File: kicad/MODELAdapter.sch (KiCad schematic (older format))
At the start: 0 parts

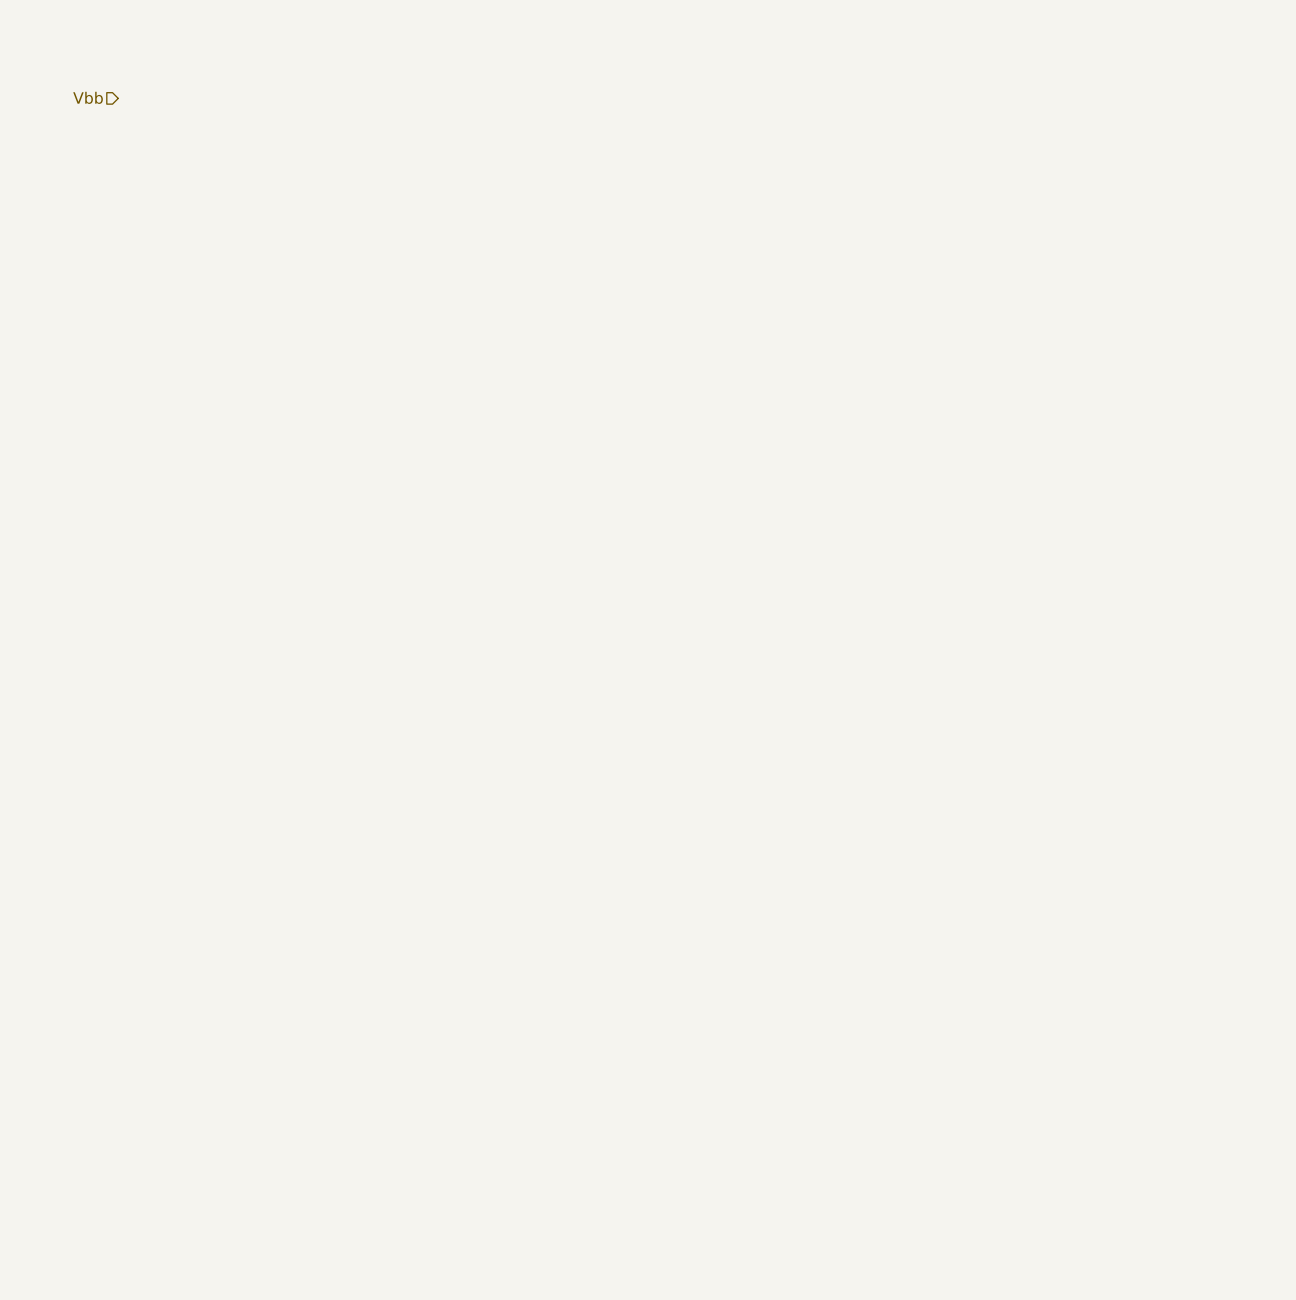
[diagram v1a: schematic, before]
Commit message: Added some more detail and moved the display from SPI to I2C
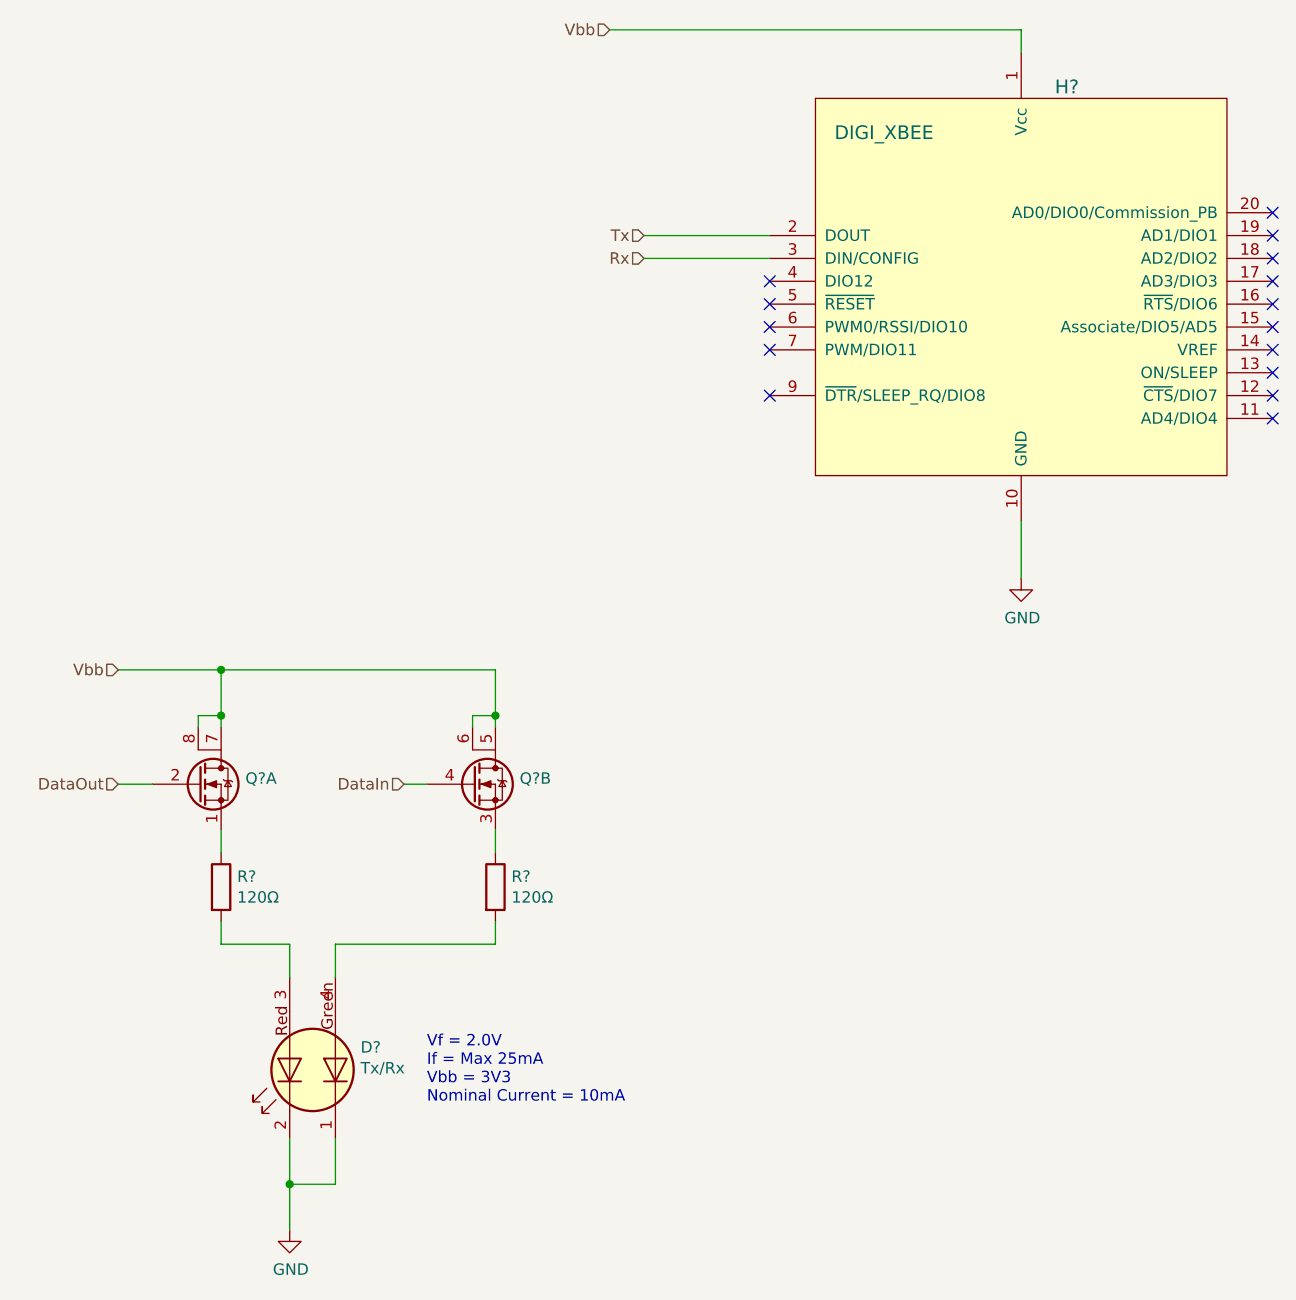
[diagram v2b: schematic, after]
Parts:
- added D?: Tx/Rx, symbol FieldDevice_R2:LED_Dual_CCAA
- added H?: DIGI_XBEE, symbol FieldDevice_R2:DIGI_XBEE
- added Q? (x2): Q_DUAL_NMOS_G2D78S1G4D56S3, symbol FieldDevice_R2:Q_DUAL_NMOS_G2D78S1G4D56S3
- added R? (x2): 120Ω, symbol Device:R
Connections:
- net Vbb: now also H?.1 (Vcc), Q?.5 (D), Q?.6 (D), Q?.7 (D), Q?.8 (D)
- new net: Q?.1 (S), R?.1
- new net: D?.3 (K1), R?.2
- new net: Q?.3 (S), R?.1
- new net: D?.4 (K2), R?.2
- new net DataIn: Q?.4 (G)
- new net DataOut: Q?.2 (G)
- new net GND: D?.1 (A1), D?.2 (A2), H?.10 (GND)
- new net Rx: H?.3 (DIN/CONFIG)
- new net Tx: H?.2 (DOUT)
- no-connect marks 0 -> 15
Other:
- note added: "Vf = 2.0V\nIf = Max 25mA\nVbb = 3V3\nNominal Current = 10mA"
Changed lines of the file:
@@
 EESchema Schematic File Version 4
 LIBS:FieldDevice_R2-cache
-LIBS:FieldDevice_Power_5V-cache
-EELAYER 26 0
+EELAYER 29 0
 EELAYER END
 $Descr A4 11693 8268
 encoding utf-8
-Sheet 8 8
+Sheet 7 8
 Title ""
 Date ""
@@
 Comment4 ""
 $EndDescr
-Text HLabel 2150 1650 0    50   Input ~ 0
+Text HLabel 4300 1350 0    50   Input ~ 0
 Vbb
+Text HLabel 4450 2350 0    50   Input ~ 0
+Rx
+Text HLabel 4450 2250 0    50   Input ~ 0
+Tx
+$Comp
+L FieldDevice_R2:DIGI_XBEE H?
+U 1 1 5CBC3B62
+P 6100 2500
+F 0 "H?" H 6300 3400 60  0000 C CNN
+F 1 "DIGI_XBEE" H 5500 3200 60  0000 C CNN
+F 2 "" H 5450 2300 60  0000 C CNN
+F 3 "" H 5450 2300 60  0000 C CNN
+	1    6100 2500
+	1    0    0    -1
+$EndComp
+Wire Wire Line
+	4300 1350 6100 1350
+Wire Wire Line
+	6100 1350 6100 1450
+Wire Wire Line
+	6100 3500 6100 3750
+$Comp
+L FieldDevice_Power_5V-rescue:GND #PWR?
+U 1 1 5CBC5560
+P 6100 3750
+F 0 "#PWR?" H 6100 3500 50  0001 C CNN
+F 1 "GND" H 6105 3577 50  0000 C CNN
+F 2 "" H 6100 3750 50  0001 C CNN
+F 3 "" H 6100 3750 50  0001 C CNN
+	1    6100 3750
+	1    0    0    -1
+$EndComp
+Wire Wire Line
+	5000 2250 4450 2250
+Wire Wire Line
+	5000 2350 4450 2350
+NoConn ~ 5000 2450
+NoConn ~ 5000 2550
+NoConn ~ 5000 2650
+NoConn ~ 5000 2750
+NoConn ~ 5000 2950
+NoConn ~ 7200 3050
+NoConn ~ 7200 2950
+NoConn ~ 7200 2850
+NoConn ~ 7200 2750
+NoConn ~ 7200 2650
+NoConn ~ 7200 2550
+NoConn ~ 7200 2450
+NoConn ~ 7200 2350
+NoConn ~ 7200 2250
+NoConn ~ 7200 2150
+Text HLabel 2150 4150 0    50   Input ~ 0
+Vbb
+Wire Wire Line
+	2150 4150 2600 4150
+Wire Wire Line
+	2600 4150 2600 4350
+Wire Wire Line
+	2600 4150 3800 4150
+Wire Wire Line
+	3800 4150 3800 4350
+Connection ~ 2600 4150
+$Comp
+L Device:R R?
+U 1 1 5CBCC41D
+P 2600 5100
+F 0 "R?" H 2670 5146 50  0000 L CNN
+F 1 "120Ω" H 2670 5055 50  0000 L CNN
+F 2 "" V 2530 5100 50  0001 C CNN
+F 3 "~" H 2600 5100 50  0001 C CNN
+	1    2600 5100
+	1    0    0    -1
+$EndComp
+$Comp
+L Device:R R?
+U 1 1 5CBCCB57
+P 3800 5100
+F 0 "R?" H 3870 5146 50  0000 L CNN
+F 1 "120Ω" H 3870 5055 50  0000 L CNN
+F 2 "" V 3730 5100 50  0001 C CNN
+F 3 "~" H 3800 5100 50  0001 C CNN
+	1    3800 5100
+	1    0    0    -1
+$EndComp
+$Comp
+L FieldDevice_R2:LED_Dual_CCAA D?
+U 1 1 5CBD6344
+P 3000 5900
+F 0 "D?" V 3099 5690 50  0000 R CNN
+F 1 "Tx/Rx" V 3008 5690 50  0000 R CNN
+F 2 "" H 2970 5900 50  0001 C CNN
+F 3 "https://cdn-reichelt.de/documents/datenblatt/A500/15-22SURSYGC-S530-A3-E2-TR8_ENG_TDS.pdf" H 2970 5900 50  0001 C CNN
+F 4 "EVL 15-22SURSYG" H 3000 5900 50  0001 C CNN "MPN"
+F 5 "https://www.reichelt.de/led-smd-1210-rot-gruen-54-mcd-120-evl-15-22sursyg-p232060.html?&trstct=pol_1" H 3000 5900 50  0001 C CNN "Link"
+	1    3000 5900
+	0    -1   -1   0
+$EndComp
+$Comp
+L FieldDevice_Power_5V-rescue:GND #PWR?
+U 1 1 5CBC9016
+P 2900 6600
+F 0 "#PWR?" H 2900 6350 50  0001 C CNN
+F 1 "GND" H 2905 6427 50  0000 C CNN
+F 2 "" H 2900 6600 50  0001 C CNN
+F 3 "" H 2900 6600 50  0001 C CNN
+	1    2900 6600
+	1    0    0    -1
+$EndComp
+Wire Wire Line
+	2900 6200 2900 6400
+Wire Wire Line
+	3100 6200 3100 6400
+Wire Wire Line
+	3100 6400 2900 6400
+Connection ~ 2900 6400
+Wire Wire Line
+	2900 6400 2900 6600
+Wire Wire Line
+	2600 5250 2600 5350
+Wire Wire Line
+	2600 5350 2900 5350
+Wire Wire Line
+	3100 5350 3800 5350
+Wire Wire Line
+	3800 5350 3800 5250
+Wire Wire Line
+	2900 5495 2900 5350
+Wire Wire Line
+	3100 5495 3100 5350
+Wire Wire Line
+	3500 4650 3400 4650
+Wire Wire Line
+	2300 4650 2150 4650
+Text HLabel 2150 4650 0    50   Input ~ 0
+DataOut
+Text HLabel 3400 4650 0    50   Input ~ 0
+DataIn
+$Comp
+L FieldDevice_R2:Q_DUAL_NMOS_G2D78S1G4D56S3 Q?
+U 1 1 5CBC91E5
+P 2500 4650
+F 0 "Q?" H 2706 4675 50  0000 L CNN
+F 1 "Q_DUAL_NMOS_G2D78S1G4D56S3" H 2706 4630 50  0001 L CNN
+F 2 "" H 2700 4650 50  0001 C CNN
+F 3 "https://cdn-reichelt.de/documents/datenblatt/A200/TSM9926DCS.pdf" H 2700 4650 50  0001 C CNN
+F 4 "TSM9926DCS " H 2500 4650 50  0001 C CNN "MPN"
+F 5 "https://www.reichelt.de/mosfet-2xn-ch-20v-6a-0-03r-so8-tsm9926dcs-p254992.html?&trstct=pol_0" H 2500 4650 50  0001 C CNN "Link"
+	1    2500 4650
+	1    0    0    -1
+$EndComp
+Wire Wire Line
+	2600 4850 2600 4950
+Wire Wire Line
+	2500 4400 2500 4350
+Wire Wire Line
+	2500 4350 2600 4350
+Connection ~ 2600 4350
+Wire Wire Line
+	2600 4350 2600 4400
+$Comp
+L FieldDevice_R2:Q_DUAL_NMOS_G2D78S1G4D56S3 Q?
+U 2 1 5CBCC7E8
+P 3700 4650
+F 0 "Q?" H 3906 4675 50  0000 L CNN
+F 1 "Q_DUAL_NMOS_G2D78S1G4D56S3" H 3906 4630 50  0001 L CNN
+F 2 "" H 3900 4650 50  0001 C CNN
+F 3 "https://cdn-reichelt.de/documents/datenblatt/A200/TSM9926DCS.pdf" H 3900 4650 50  0001 C CNN
+F 4 "TSM9926DCS " H 3700 4650 50  0001 C CNN "MPN"
+F 5 "https://www.reichelt.de/mosfet-2xn-ch-20v-6a-0-03r-so8-tsm9926dcs-p254992.html?&trstct=pol_0" H 3700 4650 50  0001 C CNN "Link"
+	2    3700 4650
+	1    0    0    -1
+$EndComp
+Wire Wire Line
+	3700 4400 3700 4350
+Wire Wire Line
+	3700 4350 3800 4350
+Connection ~ 3800 4350
+Wire Wire Line
+	3800 4350 3800 4400
+Wire Wire Line
+	3800 4850 3800 4950
+Text Notes 3500 6050 0    50   ~ 0
+Vf = 2.0V\nIf = Max 25mA\nVbb = 3V3\nNominal Current = 10mA
 $EndSCHEMATC

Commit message: Revision 3
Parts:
- D?: Link https://www.reichelt.de/led-smd-1210-rot-gruen-54-mcd-120-e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 -> https://www.digikey.de/product-detail/de/lumex-opto-compone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; MPN EVL 15-22SURSYG -> SML-LX15IGC-RP-TR
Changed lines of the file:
@@
 Comment4 ""
 $EndDescr
-Text HLabel 4300 1350 0    50   Input ~ 0
+Text HLabel 5600 1350 0    50   Input ~ 0
 Vbb
 Text HLabel 4450 2350 0    50   Input ~ 0
@@
 $EndComp
 Wire Wire Line
-	4300 1350 6100 1350
+	5600 1350 6100 1350
 Wire Wire Line
 	6100 1350 6100 1450
@@
 F 1 "Tx/Rx" V 3008 5690 50  0000 R CNN
 F 2 "" H 2970 5900 50  0001 C CNN
-F 3 "https://cdn-reichelt.de/documents/datenblatt/A500/15-22SURSYGC-S530-A3-E2-TR8_ENG_TDS.pdf" H 2970 5900 50  0001 C CNN
-F 4 "EVL 15-22SURSYG" H 3000 5900 50  0001 C CNN "MPN"
-F 5 "https://www.reichelt.de/led-smd-1210-rot-gruen-54-mcd-120-evl-15-22sursyg-p232060.html?&trstct=pol_1" H 3000 5900 50  0001 C CNN "Link"
+F 3 "https://www.lumex.com/spec/SML-LX15IGC-RP-TR.pdf" H 2970 5900 50  0001 C CNN
+F 4 "SML-LX15IGC-RP-TR	" H 3000 5900 50  0001 C CNN "MPN"
+F 5 "https://www.digikey.de/product-detail/de/lumex-opto-components-inc/SML-LX15IGC-RP-TR/67-1655-6-ND/1754501" H 3000 5900 50  0001 C CNN "Link"
 	1    3000 5900
 	0    -1   -1   0

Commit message: Updates and testing
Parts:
- removed Q? (x2): Q_DUAL_NMOS_G2D78S1G4D56S3, symbol FieldDevice_R2:Q_DUAL_NMOS_G2D78S1G4D56S3
- added Q? (x2): Q_DUAL_PMOS_TSM9933DCS, symbol FieldDevice_R2:Q_DUAL_PMOS_TSM9933DCS
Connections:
- net DataIn: now also Q?.4 (G)
- net DataOut: now also Q?.2 (G)
- net Vbb: now also Q?.1 (S), Q?.3 (S)
- net at R?.1: now also Q?.7 (D), Q?.8 (D)
- net at R?.1: now also Q?.5 (D), Q?.6 (D)
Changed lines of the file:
@@
 	2150 4150 2600 4150
 Wire Wire Line
-	2600 4150 2600 4350
-Wire Wire Line
 	2600 4150 3800 4150
-Wire Wire Line
-	3800 4150 3800 4350
 Connection ~ 2600 4150
 $Comp
@@
 	3100 5495 3100 5350
 Wire Wire Line
-	3500 4650 3400 4650
+	2300 4600 2150 4600
+Text HLabel 2150 4600 0    50   Input ~ 0
+DataOut
+Text HLabel 3350 4600 0    50   Input ~ 0
+DataIn
 Wire Wire Line
-	2300 4650 2150 4650
-Text HLabel 2150 4650 0    50   Input ~ 0
-DataOut
-Text HLabel 3400 4650 0    50   Input ~ 0
-DataIn
+	2600 4850 2600 4900
+Wire Wire Line
+	3800 4850 3800 4900
+Text Notes 3500 6050 0    50   ~ 0
+Vf = 2.0V\nIf = Max 25mA\nVbb = 3V3\nNominal Current = 10mA
 $Comp
-L FieldDevice_R2:Q_DUAL_NMOS_G2D78S1G4D56S3 Q?
-U 1 1 5CBC91E5
-P 2500 4650
-F 0 "Q?" H 2706 4675 50  0000 L CNN
-F 1 "Q_DUAL_NMOS_G2D78S1G4D56S3" H 2706 4630 50  0001 L CNN
-F 2 "" H 2700 4650 50  0001 C CNN
-F 3 "https://cdn-reichelt.de/documents/datenblatt/A200/TSM9926DCS.pdf" H 2700 4650 50  0001 C CNN
-F 4 "TSM9926DCS " H 2500 4650 50  0001 C CNN "MPN"
-F 5 "https://www.reichelt.de/mosfet-2xn-ch-20v-6a-0-03r-so8-tsm9926dcs-p254992.html?&trstct=pol_0" H 2500 4650 50  0001 C CNN "Link"
-	1    2500 4650
+L FieldDevice_R2:Q_DUAL_PMOS_TSM9933DCS Q?
+U 1 1 5D6B0A26
+P 2500 4600
+F 0 "Q?" H 2788 4575 50  0000 L CNN
+F 1 "Q_DUAL_PMOS_TSM9933DCS" H 2788 4530 50  0001 L CNN
+F 2 "" H 2550 4600 50  0001 C CNN
+F 3 "https://cdn-reichelt.de/documents/datenblatt/A200/TSM9933DCS.pdf" H 2550 4600 50  0001 C CNN
+F 4 "TSM9933DCS" H 2500 4600 50  0001 C CNN "MPN"
+F 5 "https://www.reichelt.de/mosfet-2xp-ch-20v-4-7a-0-06r-so8-tsm9933dcs-p254993.html?&trstct=pol_0" H 2500 4600 50  0001 C CNN "Link"
+	1    2500 4600
+	1    0    0    -1
+$EndComp
+$Comp
+L FieldDevice_R2:Q_DUAL_PMOS_TSM9933DCS Q?
+U 2 1 5D6B2369
+P 3700 4600
+F 0 "Q?" H 3988 4575 50  0000 L CNN
+F 1 "Q_DUAL_PMOS_TSM9933DCS" H 3988 4530 50  0001 L CNN
+F 2 "" H 3750 4600 50  0001 C CNN
+F 3 "https://cdn-reichelt.de/documents/datenblatt/A200/TSM9933DCS.pdf" H 3750 4600 50  0001 C CNN
+F 4 "TSM9933DCS" H 3700 4600 50  0001 C CNN "MPN"
+F 5 "https://www.reichelt.de/mosfet-2xp-ch-20v-4-7a-0-06r-so8-tsm9933dcs-p254993.html?&trstct=pol_0" H 3700 4600 50  0001 C CNN "Link"
+	2    3700 4600
 	1    0    0    -1
 $EndComp
 Wire Wire Line
-	2600 4850 2600 4950
+	3350 4600 3500 4600
 Wire Wire Line
-	2500 4400 2500 4350
+	2600 4150 2600 4400
 Wire Wire Line
-	2500 4350 2600 4350
-Connection ~ 2600 4350
+	3800 4150 3800 4400
 Wire Wire Line
-	2600 4350 2600 4400
-$Comp
-L FieldDevice_R2:Q_DUAL_NMOS_G2D78S1G4D56S3 Q?
-U 2 1 5CBCC7E8
-P 3700 4650
-F 0 "Q?" H 3906 4675 50  0000 L CNN
-F 1 "Q_DUAL_NMOS_G2D78S1G4D56S3" H 3906 4630 50  0001 L CNN
-F 2 "" H 3900 4650 50  0001 C CNN
-F 3 "https://cdn-reichelt.de/documents/datenblatt/A200/TSM9926DCS.pdf" H 3900 4650 50  0001 C CNN
-F 4 "TSM9926DCS " H 3700 4650 50  0001 C CNN "MPN"
-F 5 "https://www.reichelt.de/mosfet-2xn-ch-20v-6a-0-03r-so8-tsm9926dcs-p254992.html?&trstct=pol_0" H 3700 4650 50  0001 C CNN "Link"
-	2    3700 4650
-	1    0    0    -1
-$EndComp
+	2600 4900 2700 4900
 Wire Wire Line
-	3700 4400 3700 4350
+	2700 4900 2700 4850
+Connection ~ 2600 4900
 Wire Wire Line
-	3700 4350 3800 4350
-Connection ~ 3800 4350
+	2600 4900 2600 4950
 Wire Wire Line
-	3800 4350 3800 4400
+	3800 4900 3900 4900
 Wire Wire Line
-	3800 4850 3800 4950
-Text Notes 3500 6050 0    50   ~ 0
-Vf = 2.0V\nIf = Max 25mA\nVbb = 3V3\nNominal Current = 10mA
+	3900 4900 3900 4850
+Connection ~ 3800 4900
+Wire Wire Line
+	3800 4900 3800 4950
 $EndSCHEMATC
